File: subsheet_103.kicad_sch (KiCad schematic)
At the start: 0 parts

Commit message: done subsheet 100 : CPU
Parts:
- added I48: PERIPHERAL_INTERFACE_ADAPTER_PHY, Package_DIP:DIP-40_W15.24mm_LongPads, symbol mc6821p:PERIPHERAL_INTERFACE_ADAPTER_PHY
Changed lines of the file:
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@@
     (rev "DRAFT")
   )
+  (symbol (lib_id "mc6821p:PERIPHERAL_INTERFACE_ADAPTER_PHY") (at 101.6 100.33 0) (unit 1)
+    (in_bom yes) (on_board yes)
+    (property "Reference" "I48" (id 0) (at 91.44 68.58 0)
+      (effects (font (size 1.27 1.27)) (justify left top))
+    )
+    (property "Value" "PERIPHERAL_INTERFACE_ADAPTER_PHY" (id 1) (at 91.44 71.12 0)
+      (effects (font (size 1.27 1.27) bold) (justify left top))
+    )
+    (property "Footprint" "Package_DIP:DIP-40_W15.24mm_LongPads" (id 2) (at 91.44 66.04 0)
+      (effects (font (size 1.27 1.27)) (justify left top) hide)
+    )
+    (property "Datasheet" "https://d148k72crfmm2d.cloudfront.net/wp-content/uploads/2017/02/MC6821P.pdf" (id 3) (at 91.44 63.5 0)
+      (effects (font (size 1.27 1.27)) (justify left top) hide)
+    )
+    (pin "1")
+    (pin "10")
+    (pin "11")
+    (pin "12")
+    (pin "13")
+    (pin "14")
+    (pin "15")
+    (pin "16")
+    (pin "17")
+    (pin "18")
+    (pin "19")
+    (pin "2")
+    (pin "20")
+    (pin "21")
+    (pin "22")
+    (pin "23")
+    (pin "24")
+    (pin "25")
+    (pin "26")
+    (pin "27")
+    (pin "28")
+    (pin "29")
+    (pin "3")
+    (pin "30")
+    (pin "31")
+    (pin "32")
+    (pin "33")
+    (pin "34")
+    (pin "35")
+    (pin "36")
+    (pin "37")
+    (pin "38")
+    (pin "39")
+    (pin "4")
+    (pin "40")
+    (pin "5")
+    (pin "6")
+    (pin "7")
+    (pin "8")
+    (pin "9")
+  )
 )

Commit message: information schéma, commence le gate array I29
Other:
- title: (none) -> Conversion du Thomson MO5 — Unité centrale
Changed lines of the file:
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@@
   (paper "A4" portrait)
   (title_block
+    (title "Conversion du Thomson MO5 — Unité centrale")
     (date "2023-05-12")
     (rev "DRAFT")
+    (comment 1 "http://github.com/sporniket/kicad-conversions--thomson-mo5--v1")
+    (comment 2 "Dépôt d'origine : ")
+    (comment 4 "Reference : POP5001 501994-01")
   )
   (symbol (lib_id "mc6821p:PERIPHERAL_INTERFACE_ADAPTER_PHY") (at 101.6 100.33 0) (unit 1)

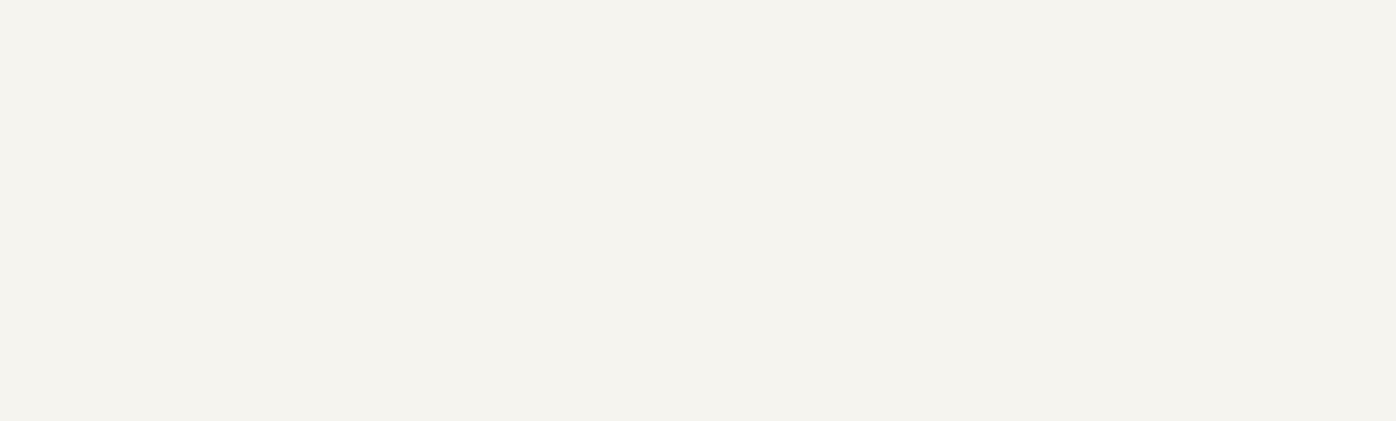
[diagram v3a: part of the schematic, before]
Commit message: bouge les composants de référence vers la feuille du pia
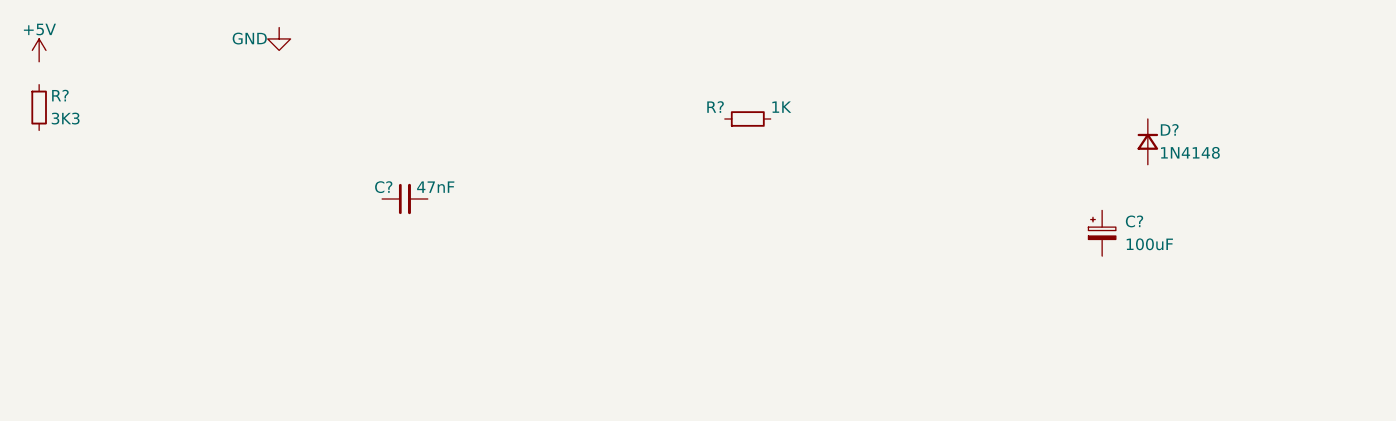
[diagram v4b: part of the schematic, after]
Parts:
- added C?: 100uF, symbol Device:C_Polarized_Small
- added C?: 47nF, symbol Device:C_Small
- added D?: 1N4148, symbol Device:D_Small
- added R?: 1K, symbol Device:R_Small
- added R?: 3K3, symbol Device:R_Small
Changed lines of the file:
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@@
     (comment 4 "Reference : POP5001 501994-01")
+  )
+  (symbol (lib_id "Device:R_Small") (at 50.8 -38.1 90) (unit 1)
+    (in_bom yes) (on_board yes)
+    (property "Reference" "R?" (id 0) (at 48.26 -39.37 90)
+      (effects (font (size 1.27 1.27)) (justify left))
+    )
+    (property "Value" "1K" (id 1) (at 53.34 -39.37 90)
+      (effects (font (size 1.27 1.27)) (justify right))
+    )
+    (property "Footprint" "" (id 2) (at 50.8 -38.1 0)
+      (effects (font (size 1.27 1.27)) hide)
+    )
+    (property "Datasheet" "~" (id 3) (at 50.8 -38.1 0)
+      (effects (font (size 1.27 1.27)) hide)
+    )
+    (pin "1")
+    (pin "2")
+  )
+  (symbol (lib_id "Device:R_Small") (at -27.94 -39.37 0) (unit 1)
+    (in_bom yes) (on_board yes)
+    (property "Reference" "R?" (id 0) (at -26.67 -40.64 0)
+      (effects (font (size 1.27 1.27)) (justify left))
+    )
+    (property "Value" "3K3" (id 1) (at -26.67 -38.1 0)
+      (effects (font (size 1.27 1.27)) (justify left))
+    )
+    (property "Footprint" "" (id 2) (at -27.94 -39.37 0)
+      (effects (font (size 1.27 1.27)) hide)
+    )
+    (property "Datasheet" "~" (id 3) (at -27.94 -39.37 0)
+      (effects (font (size 1.27 1.27)) hide)
+    )
+    (pin "1")
+    (pin "2")
+  )
+  (symbol (lib_id "Device:C_Polarized_Small") (at 90.17 -25.4 0) (unit 1)
+    (in_bom yes) (on_board yes)
+    (property "Reference" "C?" (id 0) (at 92.71 -26.67 0)
+      (effects (font (size 1.27 1.27)) (justify left))
+    )
+    (property "Value" "100uF" (id 1) (at 92.71 -24.13 0)
+      (effects (font (size 1.27 1.27)) (justify left))
+    )
+    (property "Footprint" "" (id 2) (at 90.17 -25.4 0)
+      (effects (font (size 1.27 1.27)) hide)
+    )
+    (property "Datasheet" "~" (id 3) (at 90.17 -25.4 0)
+      (effects (font (size 1.27 1.27)) hide)
+    )
+    (pin "1")
+    (pin "2")
+  )
+  (symbol (lib_id "power:GND") (at -1.27 -48.26 0) (unit 1)
+    (in_bom yes) (on_board yes)
+    (property "Reference" "#PWR?" (id 0) (at -1.27 -41.91 0)
+      (effects (font (size 1.27 1.27)) hide)
+    )
+    (property "Value" "GND" (id 1) (at -2.54 -46.99 0)
+      (effects (font (size 1.27 1.27)) (justify right))
+    )
+    (property "Footprint" "" (id 2) (at -1.27 -48.26 0)
+      (effects (font (size 1.27 1.27)) hide)
+    )
+    (property "Datasheet" "" (id 3) (at -1.27 -48.26 0)
+      (effects (font (size 1.27 1.27)) hide)
+    )
+    (pin "1")
+  )
+  (symbol (lib_id "power:+5V") (at -27.94 -44.45 0) (unit 1)
+    (in_bom yes) (on_board yes)
+    (property "Reference" "#PWR?" (id 0) (at -27.94 -40.64 0)
+      (effects (font (size 1.27 1.27)) hide)
+    )
+    (property "Value" "+5V" (id 1) (at -27.94 -48.006 0))
+    (property "Footprint" "" (id 2) (at -27.94 -44.45 0)
+      (effects (font (size 1.27 1.27)) hide)
+    )
+    (property "Datasheet" "" (id 3) (at -27.94 -44.45 0)
+      (effects (font (size 1.27 1.27)) hide)
+    )
+    (pin "1")
+  )
+  (symbol (lib_id "Device:C_Small") (at 12.7 -29.21 90) (unit 1)
+    (in_bom yes) (on_board yes)
+    (property "Reference" "C?" (id 0) (at 11.43 -30.48 90)
+      (effects (font (size 1.27 1.27)) (justify left))
+    )
+    (property "Value" "47nF" (id 1) (at 13.97 -30.48 90)
+      (effects (font (size 1.27 1.27)) (justify right))
+    )
+    (property "Footprint" "" (id 2) (at 12.7 -29.21 0)
+      (effects (font (size 1.27 1.27)) hide)
+    )
+    (property "Datasheet" "~" (id 3) (at 12.7 -29.21 0)
+      (effects (font (size 1.27 1.27)) hide)
+    )
+    (pin "1")
+    (pin "2")
   )
   (symbol (lib_id "mc6821p:PERIPHERAL_INTERFACE_ADAPTER_PHY") (at 101.6 100.33 0) (unit 1)
@@
     (pin "9")
   )
+  (symbol (lib_id "Device:D_Small") (at 95.25 -35.56 270) (unit 1)
+    (in_bom yes) (on_board yes)
+    (property "Reference" "D?" (id 0) (at 96.52 -36.83 90)
+      (effects (font (size 1.27 1.27)) (justify left))
+    )
+    (property "Value" "1N4148" (id 1) (at 96.52 -34.29 90)
+      (effects (font (size 1.27 1.27)) (justify left))
+    )
+    (property "Footprint" "" (id 2) (at 95.25 -35.56 90)
+      (effects (font (size 1.27 1.27)) hide)
+    )
+    (property "Datasheet" "~" (id 3) (at 95.25 -35.56 90)
+      (effects (font (size 1.27 1.27)) hide)
+    )
+    (pin "1")
+    (pin "2")
+  )
 )

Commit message: commence PIA
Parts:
- added C08, C09, C10, C11, C16, C19, C7: 220nF, symbol Device:C_Small
- added C12, C61: 6.8nF, symbol Device:C_Small
- added C18: 10nF, symbol Device:C_Small
- added C20: 4.7uF, symbol Device:C_Polarized_Small
- added C39: 47nF, symbol Device:C_Small
- added PM01: DIN-5 Port LEP, symbol Connector:DIN-5_180degree
- added PM02: DIN-5 Port Crayon optique, symbol Connector:DIN-5_180degree
- added R48, R49, R50, R51, R56, R77: 1K, symbol Device:R_Small
- added R53: 33K, symbol Device:R_Small
- added R71: 100K, symbol Device:R_Small
- added R72: 39K, symbol Device:R_Small
- added R75: 15K, symbol Device:R_Small
- added R76: 3K9, symbol Device:R_Small
- added T11: BC 547 B, symbol Device:Q_NPN_CEB
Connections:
- net +5V: now also I48.20 (VCC), C39.1, R72.1, R76.1
- net GND: now also I48.1 (GND), C08.1, C09.1, C10.1, C11.1, C12.2, C18.2, C39.2, C61.2, PM01.2, R71.2, R75.2, R77.2
- net at I48.10 (PB0): now also R53.2
- net FORME: now reaches I48.2 (PA0)
- net R/~{W}: now reaches I48.21 (R/~{W})
- net ~{A2}: now reaches I48.22 (CS0)
- net D/NA7CX: now reaches I48.23 (~{CS2})
- net ~{A3}: now reaches I48.24 (CS1)
- net GA_E: now reaches I48.25 (E)
- net D7: now reaches I48.26 (D7)
- net D6: now reaches I48.27 (D6)
- net D5: now reaches I48.28 (D5)
- net D4: now reaches I48.29 (D4)
- net at I48.3 (PA1): now also R51.2
- net D3: now reaches I48.30 (D3)
- net D2: now reaches I48.31 (D2)
- net D1: now reaches I48.32 (D1)
- net D0: now reaches I48.33 (D0)
- net J/~{RESET}: now reaches I48.34 (~{RESET})
- net A1: now reaches I48.35 (RS1)
- net A0: now reaches I48.36 (RS0)
- net G/~{IRQ}: now reaches I48.37 (~{IRQB})
- net I/~{FIRQ}: now reaches I48.38 (~{IRQA})
- net CA2: now reaches I48.39 (CA2)
- net CA2: now also PM01.1
- net at I48.4 (PA2): now also R50.2
- net at I48.5 (PA3): now also R49.2
- net at I48.6 (PA4): now also R48.2
- net at I48.8 (PA6): now also PM01.5
- net at I48.9 (PA7): now also PM01.4, R77.1
- new net: C11.2, R51.1
- new net: C18.1, C19.2, C61.1, C7.2, R71.1, R72.2, T11.3 (B)
- new net: C16.2, R56.1
- new net: C12.1, R53.1, R56.2
- new net: C19.1, PM01.3
- new net: C09.2, R49.1
- new net: C16.1, R75.1, T11.2 (E)
- new net: C10.2, R50.1
- new net: C20.1, R76.2, T11.1 (C)
- new net: C08.2, R48.1
- new net K/SON: C7.1
- new net N/SON TV: C20.2
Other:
- note added: "Check the actual wiring DIN or in sequence"
- moved on the sheet: I48

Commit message: fin provisoire du PIA
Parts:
- removed PM02: DIN-5 Port Crayon optique, symbol Connector:DIN-5_180degree
- added B04: Port A du clavier, symbol Connector_Generic:Conn_01x08
- added B05: Port B du clavier, symbol Connector_Generic:Conn_01x08
- added C40, C41: 47nF, symbol Device:C_Small
- added I52: 74LS151 MULTIPLEXER, Package_DIP:DIP-16_W7.62mm_LongPads, symbol 74x151:DATA_SELECTOR_MULTIPLEXER_PHY
- added I53: 74LS156 DEMULTIPLEXER, Package_DIP:DIP-16_W7.62mm_LongPads, symbol 74x156:DUAL_2-LINE_TO_4-LINE_DECODERS_DEMULTIPLEXERS_PHY
- added PM02: Port crayon optique, symbol Connector_Generic:Conn_01x05
- added R74: 390, symbol Device:R_Small
- added R82: 1K, symbol Device:R_Small
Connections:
- net +5V: now also C40.1, C41.1, I52.16 (VCC), I53.16 (VCC), PM02.5 (Pin_5)
- net GND: now also C40.2, C41.2, I52.7 (~{G}), I52.8 (GND), I53.14 (~{2C}), I53.2 (~{1G}), I53.8 (GND), PM02.2 (Pin_2), R74.2, R82.2
- net at C18.1, C19.2, C61.1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: now also R75.1
- net at C16.1, T11.2 (E): no longer R75.1
- net PB1: now reaches I48.11 (PB1)
- net PB1: now also I53.13 (SEL0)
- net PB2: now reaches I48.12 (PB2)
- net PB2: now also I53.3 (SEL1)
- net at I48.13 (PB3): now also I53.1 (1C), I53.15 (~{2G})
- net at I48.14 (PB4): now also I52.11 (SEL0)
- net at I48.15 (PB5): now also I52.10 (SEL1)
- net at I48.16 (PB6): now also I52.9 (SEL2)
- net at I48.17 (PB7): now also I52.5 (Y)
- net at I48.7 (PA5): now also PM02.3 (Pin_3), R74.1
- new net: B04.1 (Pin_1), I53.9 (2Y0)
- new net: B04.2 (Pin_2), I53.10 (2Y1)
- new net: B04.3 (Pin_3), I53.11 (2Y2)
- new net: B04.4 (Pin_4), I53.12 (2Y3)
- new net 1Y0: B04.5 (Pin_5), I53.7 (1Y0)
- new net 1Y1: B04.6 (Pin_6), I53.6 (1Y1)
- new net 1Y2: B04.7 (Pin_7), I53.5 (1Y2)
- new net 1Y3: B04.8 (Pin_8), I53.4 (1Y3)
- new net B0: B05.1 (Pin_1), I52.12 (D7)
- new net B1: B05.2 (Pin_2), I52.13 (D6)
- new net B2: B05.3 (Pin_3), I52.14 (D5)
- new net B3: B05.4 (Pin_4), I52.15 (D4)
- new net B4: B05.5 (Pin_5), I52.1 (D3)
- new net B5: B05.6 (Pin_6), I52.2 (D2)
- new net B6: B05.7 (Pin_7), I52.3 (D1)
- new net B7: B05.8 (Pin_8), I52.4 (D0)
- new net OPTIC PEN 1: PM02.1 (Pin_1)
- new net OPTIC PEN 4: PM02.4 (Pin_4), R82.1
- no-connect marks 0 -> 1
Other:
- note added: "de I09-11"
- note added: "de I45-12"
- note added: "de I47-13"
- note removed: "Check the actual wiring DIN or in sequence"
- moved on the sheet: C08, C09, C10, C11, C12, C16, C18, C19, C20, C39, C61, C7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

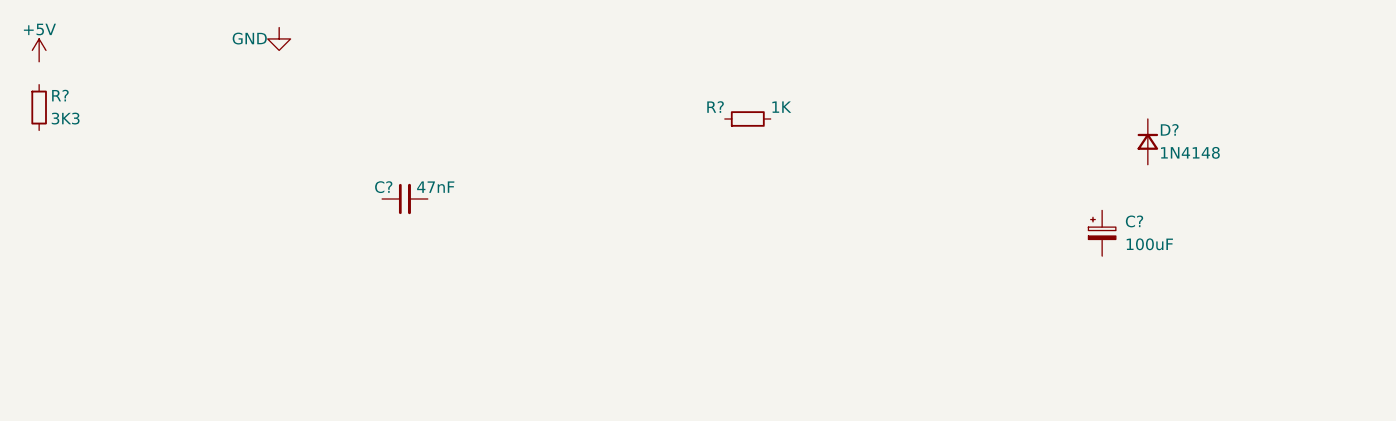
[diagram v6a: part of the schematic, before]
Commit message: RAM : drams, transceiver couleur et point
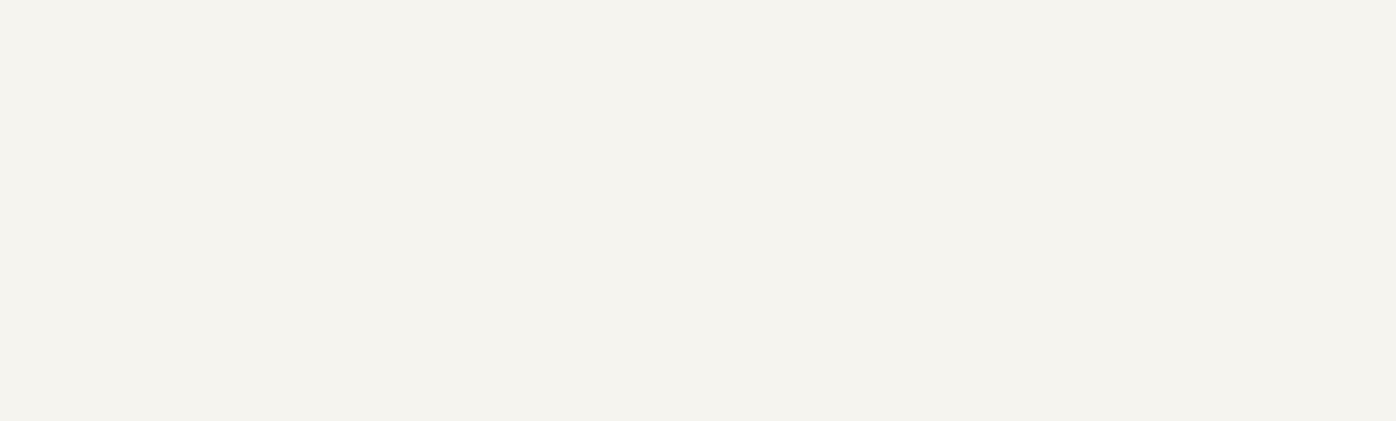
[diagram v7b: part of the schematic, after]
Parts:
- removed C?: 100uF, symbol Device:C_Polarized_Small
- removed C?: 47nF, symbol Device:C_Small
- removed D?: 1N4148, symbol Device:D_Small
- removed R?: 1K, symbol Device:R_Small
- removed R?: 3K3, symbol Device:R_Small
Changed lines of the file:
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@@
-    (pin "2")
-  )
-  (symbol (lib_id "Device:R_Small") (at 50.8 -38.1 90) (unit 1)
-    (in_bom yes) (on_board yes)
-    (property "Reference" "R?" (id 0) (at 48.26 -39.37 90)
-      (effects (font (size 1.27 1.27)) (justify left))
-    )
-    (property "Value" "1K" (id 1) (at 53.34 -39.37 90)
-      (effects (font (size 1.27 1.27)) (justify right))
-    )
-    (property "Footprint" "" (id 2) (at 50.8 -38.1 0)
-      (effects (font (size 1.27 1.27)) hide)
-    )
-    (property "Datasheet" "~" (id 3) (at 50.8 -38.1 0)
-      (effects (font (size 1.27 1.27)) hide)
-    )
-    (pin "1")
     (pin "2")
   )
@@
     (pin "2")
   )
-  (symbol (lib_id "Device:R_Small") (at -27.94 -39.37 0) (unit 1)
-    (in_bom yes) (on_board yes)
-    (property "Reference" "R?" (id 0) (at -26.67 -40.64 0)
-      (effects (font (size 1.27 1.27)) (justify left))
-    )
-    (property "Value" "3K3" (id 1) (at -26.67 -38.1 0)
-      (effects (font (size 1.27 1.27)) (justify left))
-    )
-    (property "Footprint" "" (id 2) (at -27.94 -39.37 0)
-      (effects (font (size 1.27 1.27)) hide)
-    )
-    (property "Datasheet" "~" (id 3) (at -27.94 -39.37 0)
-      (effects (font (size 1.27 1.27)) hide)
-    )
-    (pin "1")
-    (pin "2")
-  )
   (symbol (lib_id "power:+5V") (at 86.36 223.52 0) (unit 1)
     (in_bom yes) (on_board yes)
@@
     (pin "2")
   )
-  (symbol (lib_id "Device:C_Polarized_Small") (at 90.17 -25.4 0) (unit 1)
-    (in_bom yes) (on_board yes)
-    (property "Reference" "C?" (id 0) (at 92.71 -26.67 0)
-      (effects (font (size 1.27 1.27)) (justify left))
-    )
-    (property "Value" "100uF" (id 1) (at 92.71 -24.13 0)
-      (effects (font (size 1.27 1.27)) (justify left))
-    )
-    (property "Footprint" "" (id 2) (at 90.17 -25.4 0)
-      (effects (font (size 1.27 1.27)) hide)
-    )
-    (property "Datasheet" "~" (id 3) (at 90.17 -25.4 0)
-      (effects (font (size 1.27 1.27)) hide)
-    )
-    (pin "1")
-    (pin "2")
-  )
   (symbol (lib_id "Device:C_Polarized_Small") (at 118.11 227.33 90) (unit 1)
     (in_bom yes) (on_board yes)
@@
     (pin "1")
     (pin "2")
-  )
-  (symbol (lib_id "power:GND") (at -1.27 -48.26 0) (unit 1)
-    (in_bom yes) (on_board yes)
-    (property "Reference" "#PWR?" (id 0) (at -1.27 -41.91 0)
-      (effects (font (size 1.27 1.27)) hide)
-    )
-    (property "Value" "GND" (id 1) (at -2.54 -46.99 0)
-      (effects (font (size 1.27 1.27)) (justify right))
-    )
-    (property "Footprint" "" (id 2) (at -1.27 -48.26 0)
-      (effects (font (size 1.27 1.27)) hide)
-    )
-    (property "Datasheet" "" (id 3) (at -1.27 -48.26 0)
-      (effects (font (size 1.27 1.27)) hide)
-    )
-    (pin "1")
   )
   (symbol (lib_id "Device:R_Small") (at 113.03 67.31 90) (unit 1)
@@
     )
     (pin "1")
-  )
-  (symbol (lib_id "power:+5V") (at -27.94 -44.45 0) (unit 1)
-    (in_bom yes) (on_board yes)
-    (property "Reference" "#PWR?" (id 0) (at -27.94 -40.64 0)
-      (effects (font (size 1.27 1.27)) hide)
-    )
-    (property "Value" "+5V" (id 1) (at -27.94 -48.006 0))
-    (property "Footprint" "" (id 2) (at -27.94 -44.45 0)
-      (effects (font (size 1.27 1.27)) hide)
-    )
-    (property "Datasheet" "" (id 3) (at -27.94 -44.45 0)
-      (effects (font (size 1.27 1.27)) hide)
-    )
-    (pin "1")
-  )
-  (symbol (lib_id "Device:C_Small") (at 12.7 -29.21 90) (unit 1)
-    (in_bom yes) (on_board yes)
-    (property "Reference" "C?" (id 0) (at 11.43 -30.48 90)
-      (effects (font (size 1.27 1.27)) (justify left))
-    )
-    (property "Value" "47nF" (id 1) (at 13.97 -30.48 90)
-      (effects (font (size 1.27 1.27)) (justify right))
-    )
-    (property "Footprint" "" (id 2) (at 12.7 -29.21 0)
-      (effects (font (size 1.27 1.27)) hide)
-    )
-    (property "Datasheet" "~" (id 3) (at 12.7 -29.21 0)
-      (effects (font (size 1.27 1.27)) hide)
-    )
-    (pin "1")
-    (pin "2")
   )
   (symbol (lib_id "Device:Q_NPN_CEB") (at 104.14 233.68 0) (unit 1)
@@
       (effects (font (size 1.27 1.27)) hide)
     )
-    (pin "1")
-    (pin "2")
-  )
-  (symbol (lib_id "Device:D_Small") (at 95.25 -35.56 270) (unit 1)
-    (in_bom yes) (on_board yes)
-    (property "Reference" "D?" (id 0) (at 96.52 -36.83 90)
-      (effects (font (size 1.27 1.27)) (justify left))
-    )
-    (property "Value" "1N4148" (id 1) (at 96.52 -34.29 90)
-      (effects (font (size 1.27 1.27)) (justify left))
-    )
-    (property "Footprint" "" (id 2) (at 95.25 -35.56 90)
-      (effects (font (size 1.27 1.27)) hide)
-    )
-    (property "Datasheet" "~" (id 3) (at 95.25 -35.56 90)
-      (effects (font (size 1.27 1.27)) hide)
-    )
